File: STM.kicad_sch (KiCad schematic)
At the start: 0 parts

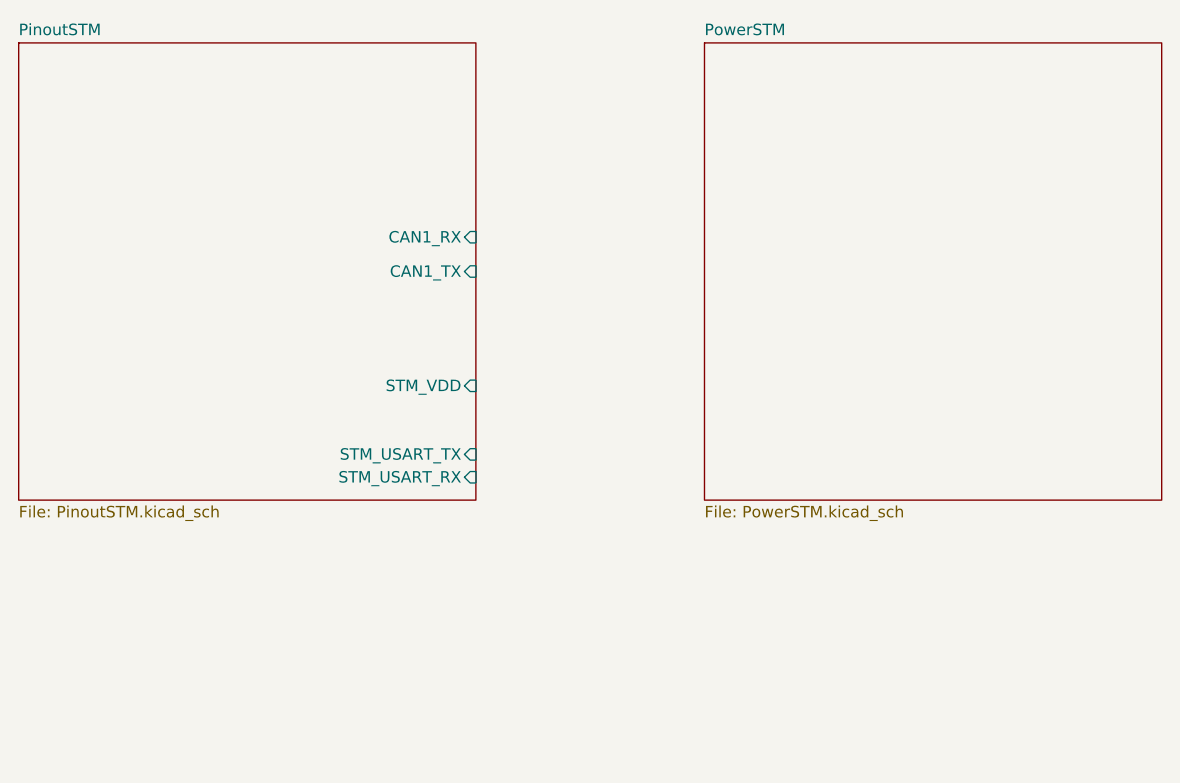
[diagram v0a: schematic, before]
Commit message: CAN tranciever
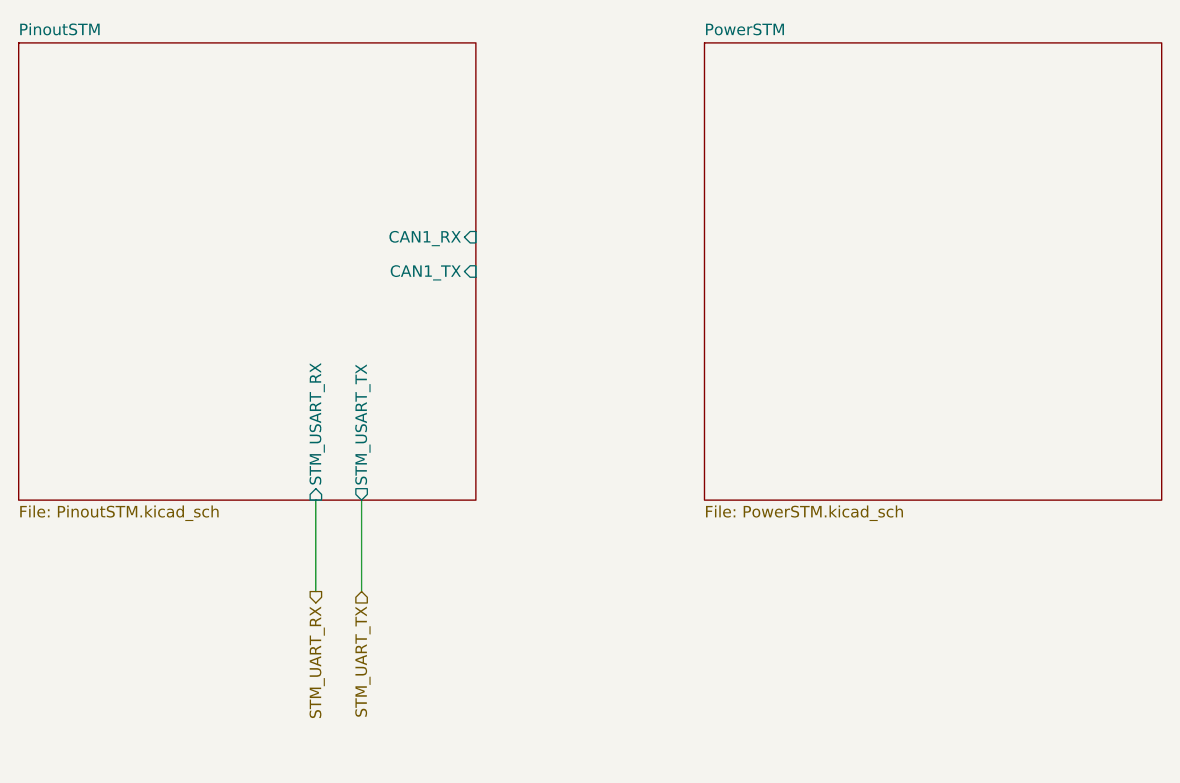
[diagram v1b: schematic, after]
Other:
- sheet PinoutSTM ports: added none; removed STM_VDD
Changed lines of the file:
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@@
 	(generator_version "9.0")
 	(paper "A4")
+	(wire
+		(pts
+			(xy 63.5 76.2) (xy 63.5 86.36)
+		)
+		(stroke
+			(width 0)
+			(type default)
+		)
+	)
+	(wire
+		(pts
+			(xy 58.42 76.2) (xy 58.42 86.36)
+		)
+		(stroke
+			(width 0)
+			(type default)
+		)
+	)
+	(hierarchical_label "STM_UART_TX"
+		(shape input)
+		(at 63.5 86.36 270)
+		(effects
+			(font
+				(size 1.27 1.27)
+			)
+			(justify right)
+		)
+	)
+	(hierarchical_label "STM_UART_RX"
+		(shape output)
+		(at 58.42 86.36 270)
+		(effects
+			(font
+				(size 1.27 1.27)
+			)
+			(justify right)
+		)
+	)
 	(sheet
 		(at 101.6 25.4)
@@
 		)
 		(pin "STM_USART_RX" input
-			(at 76.2 73.66 0)
+			(at 58.42 76.2 270)
 			(effects
 				(font
 					(size 1.27 1.27)
 				)
-				(justify right)
+				(justify left)
 			)
 		)
-		(pin "STM_USART_TX" input
-			(at 76.2 71.12 0)
+		(pin "STM_USART_TX" output
+			(at 63.5 76.2 270)
 			(effects
 				(font
 					(size 1.27 1.27)
 				)
-				(justify right)
+				(justify left)
 			)
 		)
-		(pin "STM_VDD" input
-			(at 76.2 63.5 0)
-			(effects
-				(font
-					(size 1.27 1.27)
-				)
-				(justify right)
-			)
-		)

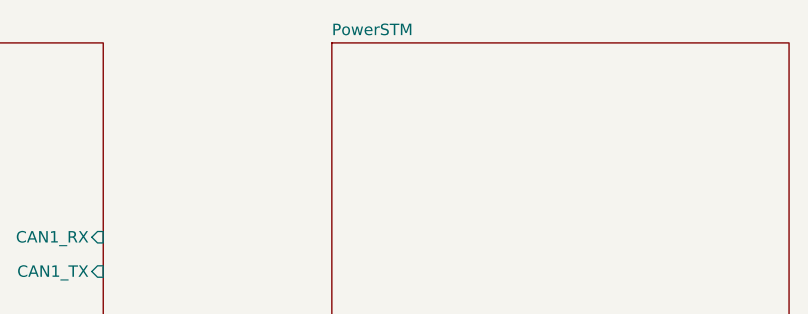
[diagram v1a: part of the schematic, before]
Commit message: Connected the Uart lines
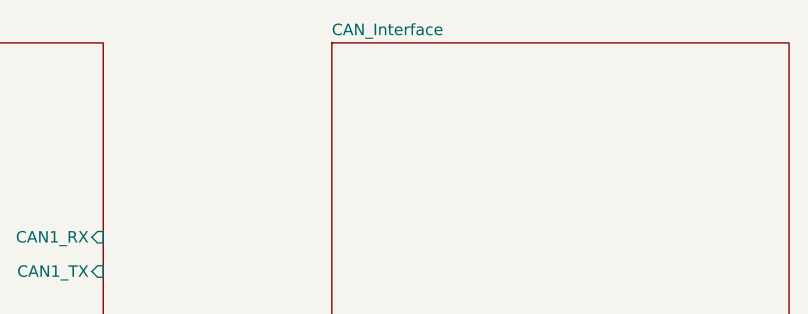
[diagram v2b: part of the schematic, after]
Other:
- sheet PowerSTM renamed CAN_Interface
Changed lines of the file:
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@@
 			(color 0 0 0 0.0000)
 		)
-		(property "Sheetname" "PowerSTM"
+		(property "Sheetname" "CAN_Interface"
 			(at 101.6 24.6884 0)
 			(effects

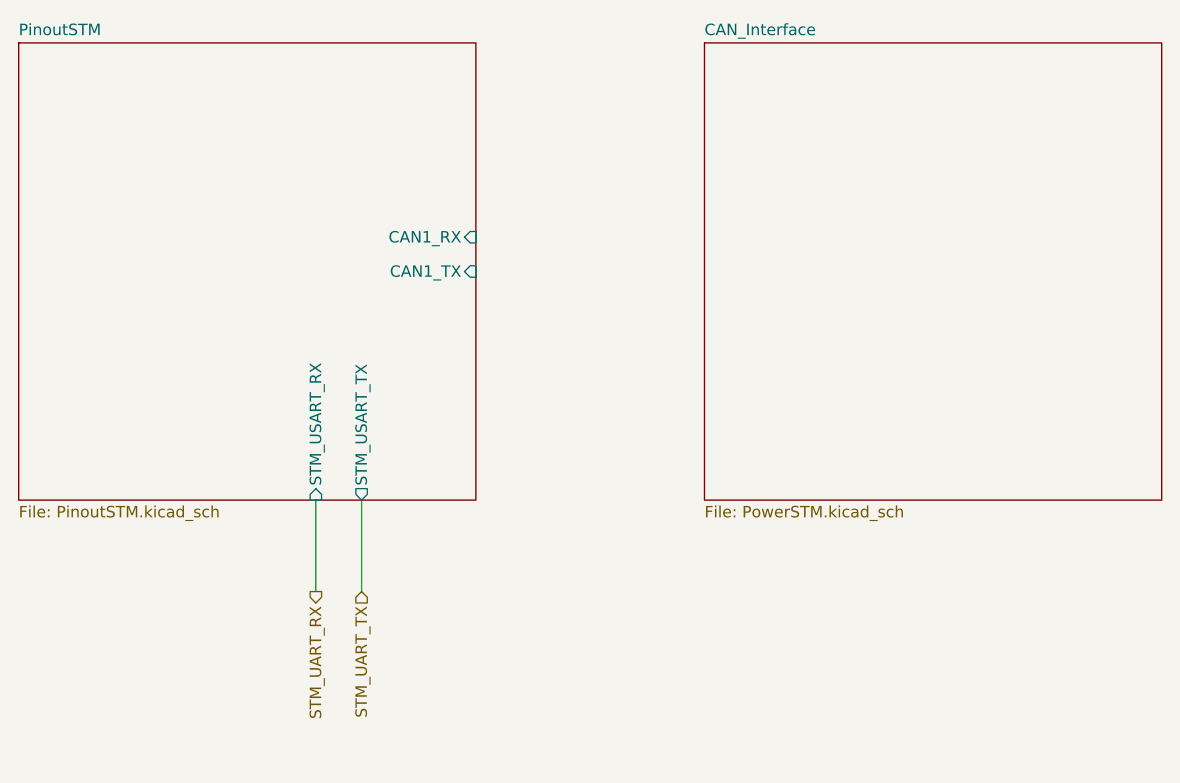
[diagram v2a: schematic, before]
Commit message: Implemented the entire can tranciever
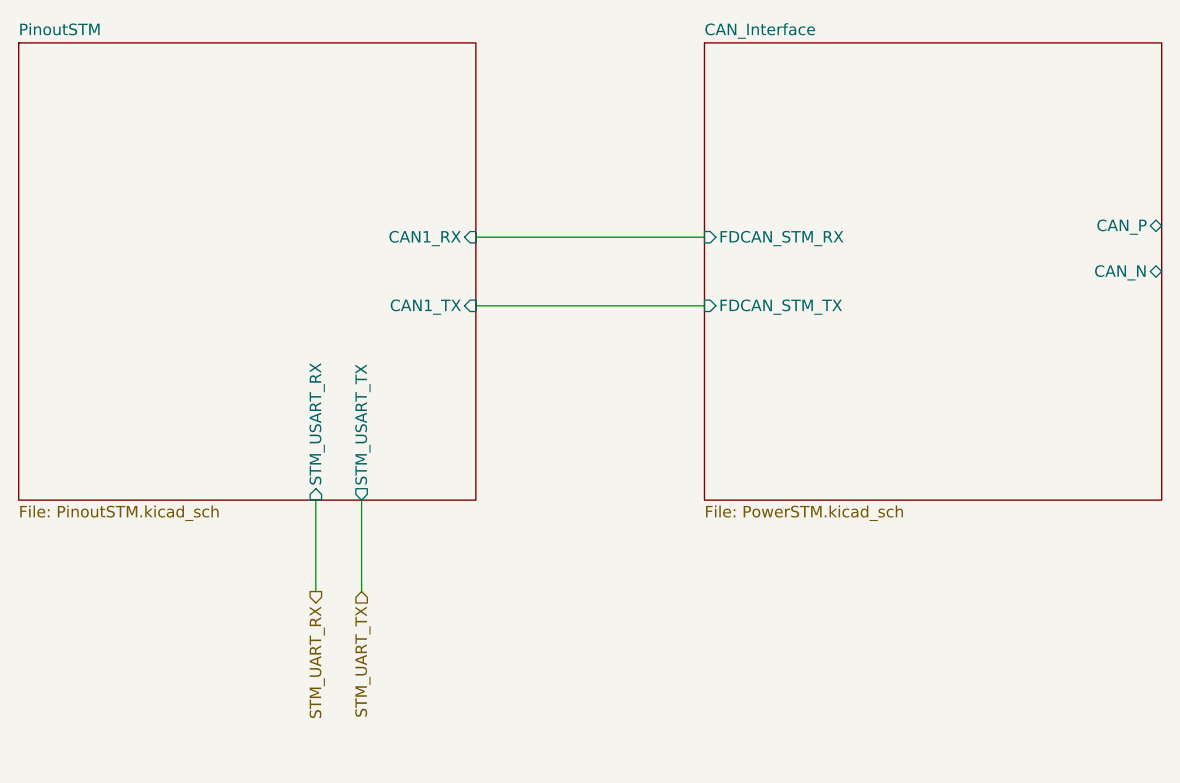
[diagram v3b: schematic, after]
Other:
- sheet CAN_Interface ports: added CAN_N, CAN_P, FDCAN_STM_RX, FDCAN_STM_TX; removed none
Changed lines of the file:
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@@
+	(wire
+		(pts
+			(xy 76.2 46.99) (xy 101.6 46.99)
+		)
+		(stroke
+			(width 0)
+			(type default)
+		)
+	)
 	(wire
 		(pts
 			(xy 58.42 76.2) (xy 58.42 86.36)
+		)
+		(stroke
+			(width 0)
+			(type default)
+		)
+	)
+	(wire
+		(pts
+			(xy 76.2 54.61) (xy 101.6 54.61)
 		)
 		(stroke
@@
 			)
 		)
+		(pin "CAN_N" bidirectional
+			(at 152.4 50.8 0)
+			(effects
+				(font
+					(size 1.27 1.27)
+				)
+				(justify right)
+			)
+		)
+		(pin "CAN_P" bidirectional
+			(at 152.4 45.72 0)
+			(effects
+				(font
+					(size 1.27 1.27)
+				)
+				(justify right)
+			)
+		)
+		(pin "FDCAN_STM_RX" input
+			(at 101.6 46.99 180)
+			(effects
+				(font
+					(size 1.27 1.27)
+				)
+				(justify left)
+			)
+		)
+		(pin "FDCAN_STM_TX" input
+			(at 101.6 54.61 180)
+			(effects
+				(font
+					(size 1.27 1.27)
+				)
+				(justify left)
+			)
+		)
 		(instances
 			(project "nautilus_mainboard"
@@
 		)
 		(pin "CAN1_TX" input
-			(at 76.2 50.8 0)
+			(at 76.2 54.61 0)
 			(effects
 				(font

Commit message: added more support for the ssd and fixed LED configuration
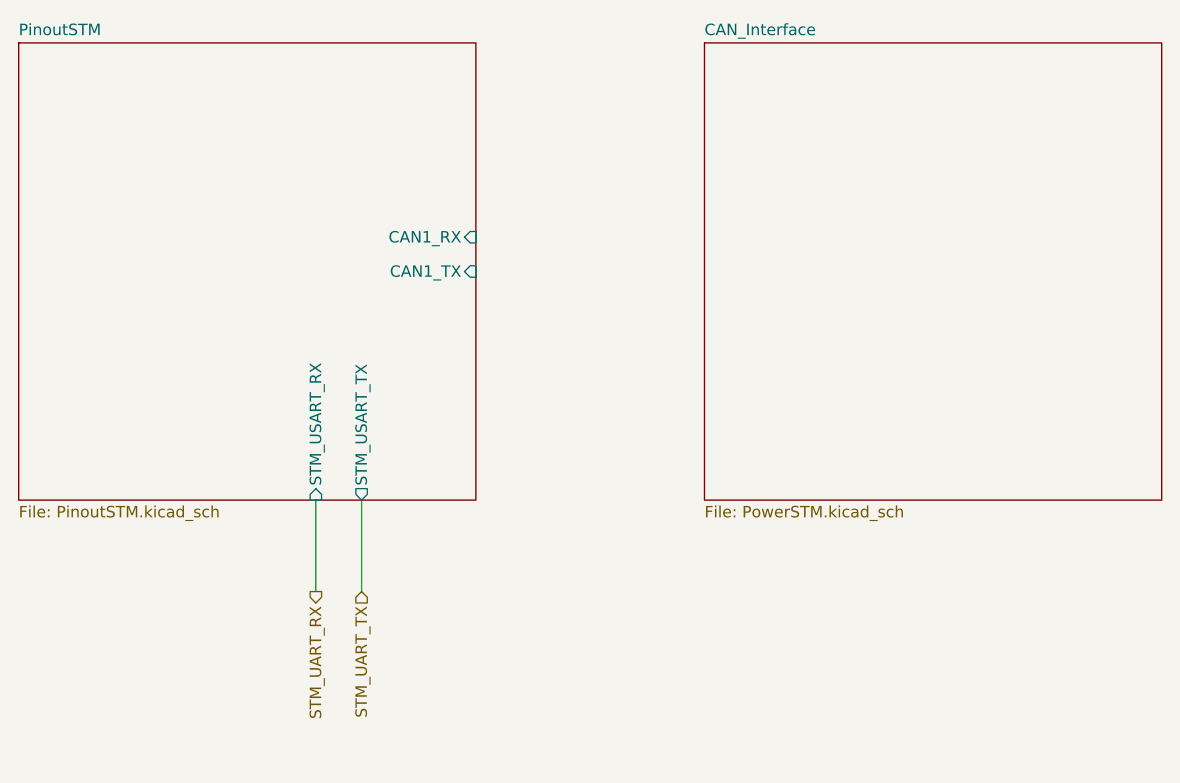
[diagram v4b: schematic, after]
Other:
- sheet CAN_Interface ports: added none; removed CAN_N, CAN_P, FDCAN_STM_RX, FDCAN_STM_TX
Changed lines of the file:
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@@
-	(wire
-		(pts
-			(xy 76.2 46.99) (xy 101.6 46.99)
-		)
-		(stroke
-			(width 0)
-			(type default)
-		)
-	)
 	(wire
 		(pts
 			(xy 58.42 76.2) (xy 58.42 86.36)
-		)
-		(stroke
-			(width 0)
-			(type default)
-		)
-	)
-	(wire
-		(pts
-			(xy 76.2 54.61) (xy 101.6 54.61)
 		)
 		(stroke
@@
 			)
 		)
-		(pin "CAN_N" bidirectional
-			(at 152.4 50.8 0)
-			(effects
-				(font
-					(size 1.27 1.27)
-				)
-				(justify right)
-			)
-		)
-		(pin "CAN_P" bidirectional
-			(at 152.4 45.72 0)
-			(effects
-				(font
-					(size 1.27 1.27)
-				)
-				(justify right)
-			)
-		)
-		(pin "FDCAN_STM_RX" input
-			(at 101.6 46.99 180)
-			(effects
-				(font
-					(size 1.27 1.27)
-				)
-				(justify left)
-			)
-		)
-		(pin "FDCAN_STM_TX" input
-			(at 101.6 54.61 180)
-			(effects
-				(font
-					(size 1.27 1.27)
-				)
-				(justify left)
-			)
-		)
 		(instances
 			(project "nautilus_mainboard"
@@
 		)
 		(pin "CAN1_TX" input
-			(at 76.2 54.61 0)
+			(at 76.2 50.8 0)
 			(effects
 				(font

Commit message: added connections for can
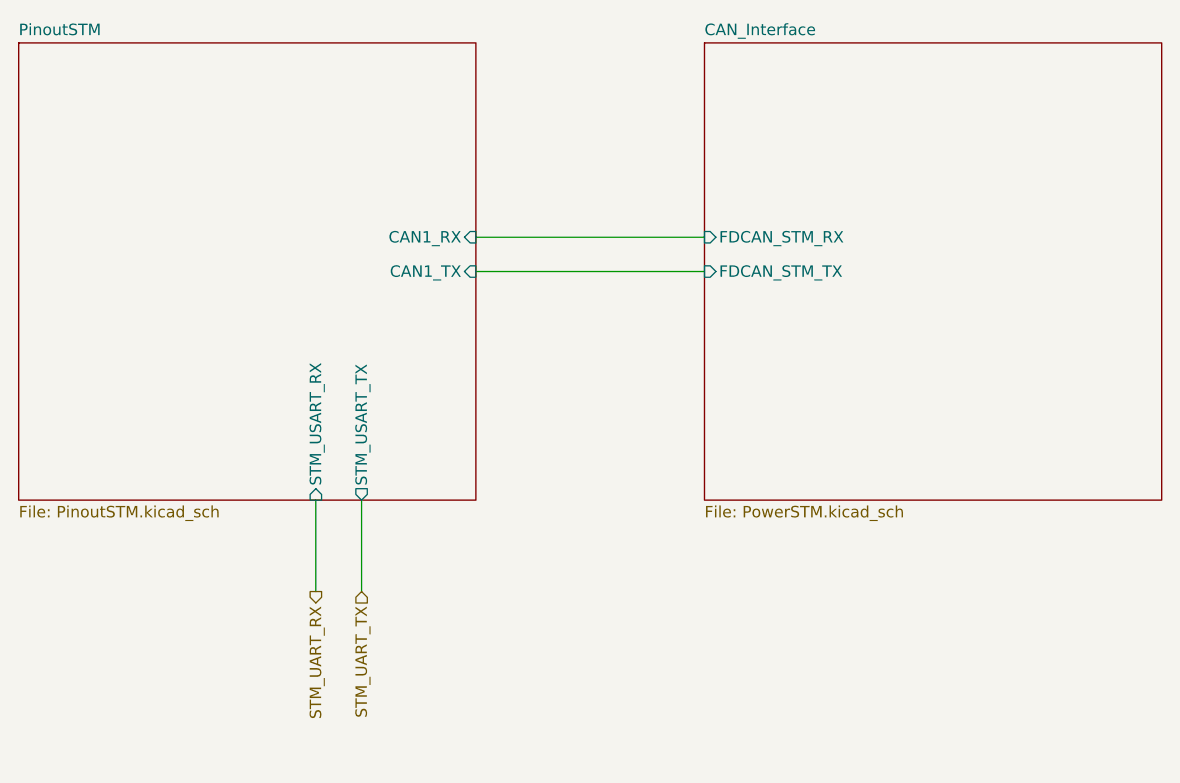
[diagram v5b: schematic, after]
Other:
- sheet CAN_Interface ports: added FDCAN_STM_RX, FDCAN_STM_TX; removed none
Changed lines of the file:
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@@
+	(wire
+		(pts
+			(xy 76.2 46.99) (xy 101.6 46.99)
+		)
+		(stroke
+			(width 0)
+			(type default)
+		)
+	)
 	(wire
 		(pts
 			(xy 63.5 76.2) (xy 63.5 86.36)
+		)
+		(stroke
+			(width 0)
+			(type default)
+		)
+	)
+	(wire
+		(pts
+			(xy 76.2 50.8) (xy 101.6 50.8)
 		)
 		(stroke
@@
 			)
 		)
+		(pin "FDCAN_STM_RX" input
+			(at 101.6 46.99 180)
+			(effects
+				(font
+					(size 1.27 1.27)
+				)
+				(justify left)
+			)
+		)
+		(pin "FDCAN_STM_TX" input
+			(at 101.6 50.8 180)
+			(effects
+				(font
+					(size 1.27 1.27)
+				)
+				(justify left)
+			)
+		)

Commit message: multiple chainges on PCB
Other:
- sheet PinoutSTM ports: added GLOBAL_EN_CM4, RUN_PG_CM4; removed none
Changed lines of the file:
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@@
+	(wire
+		(pts
+			(xy 53.34 76.2) (xy 53.34 86.36)
+		)
+		(stroke
+			(width 0)
+			(type default)
+		)
+	)
 	(wire
 		(pts
@@
 		)
 	)
+	(wire
+		(pts
+			(xy 68.58 76.2) (xy 68.58 86.36)
+		)
+		(stroke
+			(width 0)
+			(type default)
+		)
+	)
 	(hierarchical_label "STM_UART_TX"
 		(shape input)
@@
 		(shape output)
 		(at 58.42 86.36 270)
+		(effects
+			(font
+				(size 1.27 1.27)
+			)
+			(justify right)
+		)
+	)
+	(hierarchical_label "GLOBAL_EN_CM4"
+		(shape input)
+		(at 53.34 86.36 270)
+		(effects
+			(font
+				(size 1.27 1.27)
+			)
+			(justify right)
+		)
+	)
+	(hierarchical_label "RUN_PG_CM4"
+		(shape input)
+		(at 68.58 86.36 270)
 		(effects
 			(font
@@
 			(effects
 				(font
+					(size 1.27 1.27)
+				)
+				(justify left)
+			)
+		)
+		(pin "RUN_PG_CM4" input
+			(at 68.58 76.2 270)
+			(effects
+				(font
+					(size 1.27 1.27)
+				)
+				(justify left)
+			)
+		)
+		(pin "GLOBAL_EN_CM4" input
+			(at 53.34 76.2 270)
+			(effects
+				(font

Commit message: added piezzo circuit and i2c line
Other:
- sheet PinoutSTM ports: added Pack1_SCL, Pack1_SDA; removed none
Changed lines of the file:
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@@
+	(wire
+		(pts
+			(xy 36.83 76.2) (xy 36.83 86.36)
+		)
+		(stroke
+			(width 0)
+			(type default)
+		)
+	)
 	(wire
 		(pts
@@
 		(pts
 			(xy 53.34 76.2) (xy 53.34 86.36)
+		)
+		(stroke
+			(width 0)
+			(type default)
+		)
+	)
+	(wire
+		(pts
+			(xy 33.02 76.2) (xy 33.02 86.36)
 		)
 		(stroke
@@
 		(shape input)
 		(at 53.34 86.36 270)
+		(effects
+			(font
+				(size 1.27 1.27)
+			)
+			(justify right)
+		)
+	)
+	(hierarchical_label "Pack1_SCL"
+		(shape input)
+		(at 33.02 86.36 270)
+		(effects
+			(font
+				(size 1.27 1.27)
+			)
+			(justify right)
+		)
+	)
+	(hierarchical_label "Pack1_SDA"
+		(shape input)
+		(at 36.83 86.36 270)
 		(effects
 			(font
@@
 			(effects
 				(font
+					(size 1.27 1.27)
+				)
+				(justify left)
+			)
+		)
+		(pin "Pack1_SCL" input
+			(at 33.02 76.2 270)
+			(effects
+				(font
+					(size 1.27 1.27)
+				)
+				(justify left)
+			)
+		)
+		(pin "Pack1_SDA" input
+			(at 36.83 76.2 270)
+			(effects
+				(font
